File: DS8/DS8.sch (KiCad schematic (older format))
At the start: 92 parts, among them P1 CONN-02x05, Q1 3904, Q2 3904, U0 LM13700, U1 LM385, U2 LM385, U3 LM385, U4 LM385, U5 LM385, U6 KA78L05

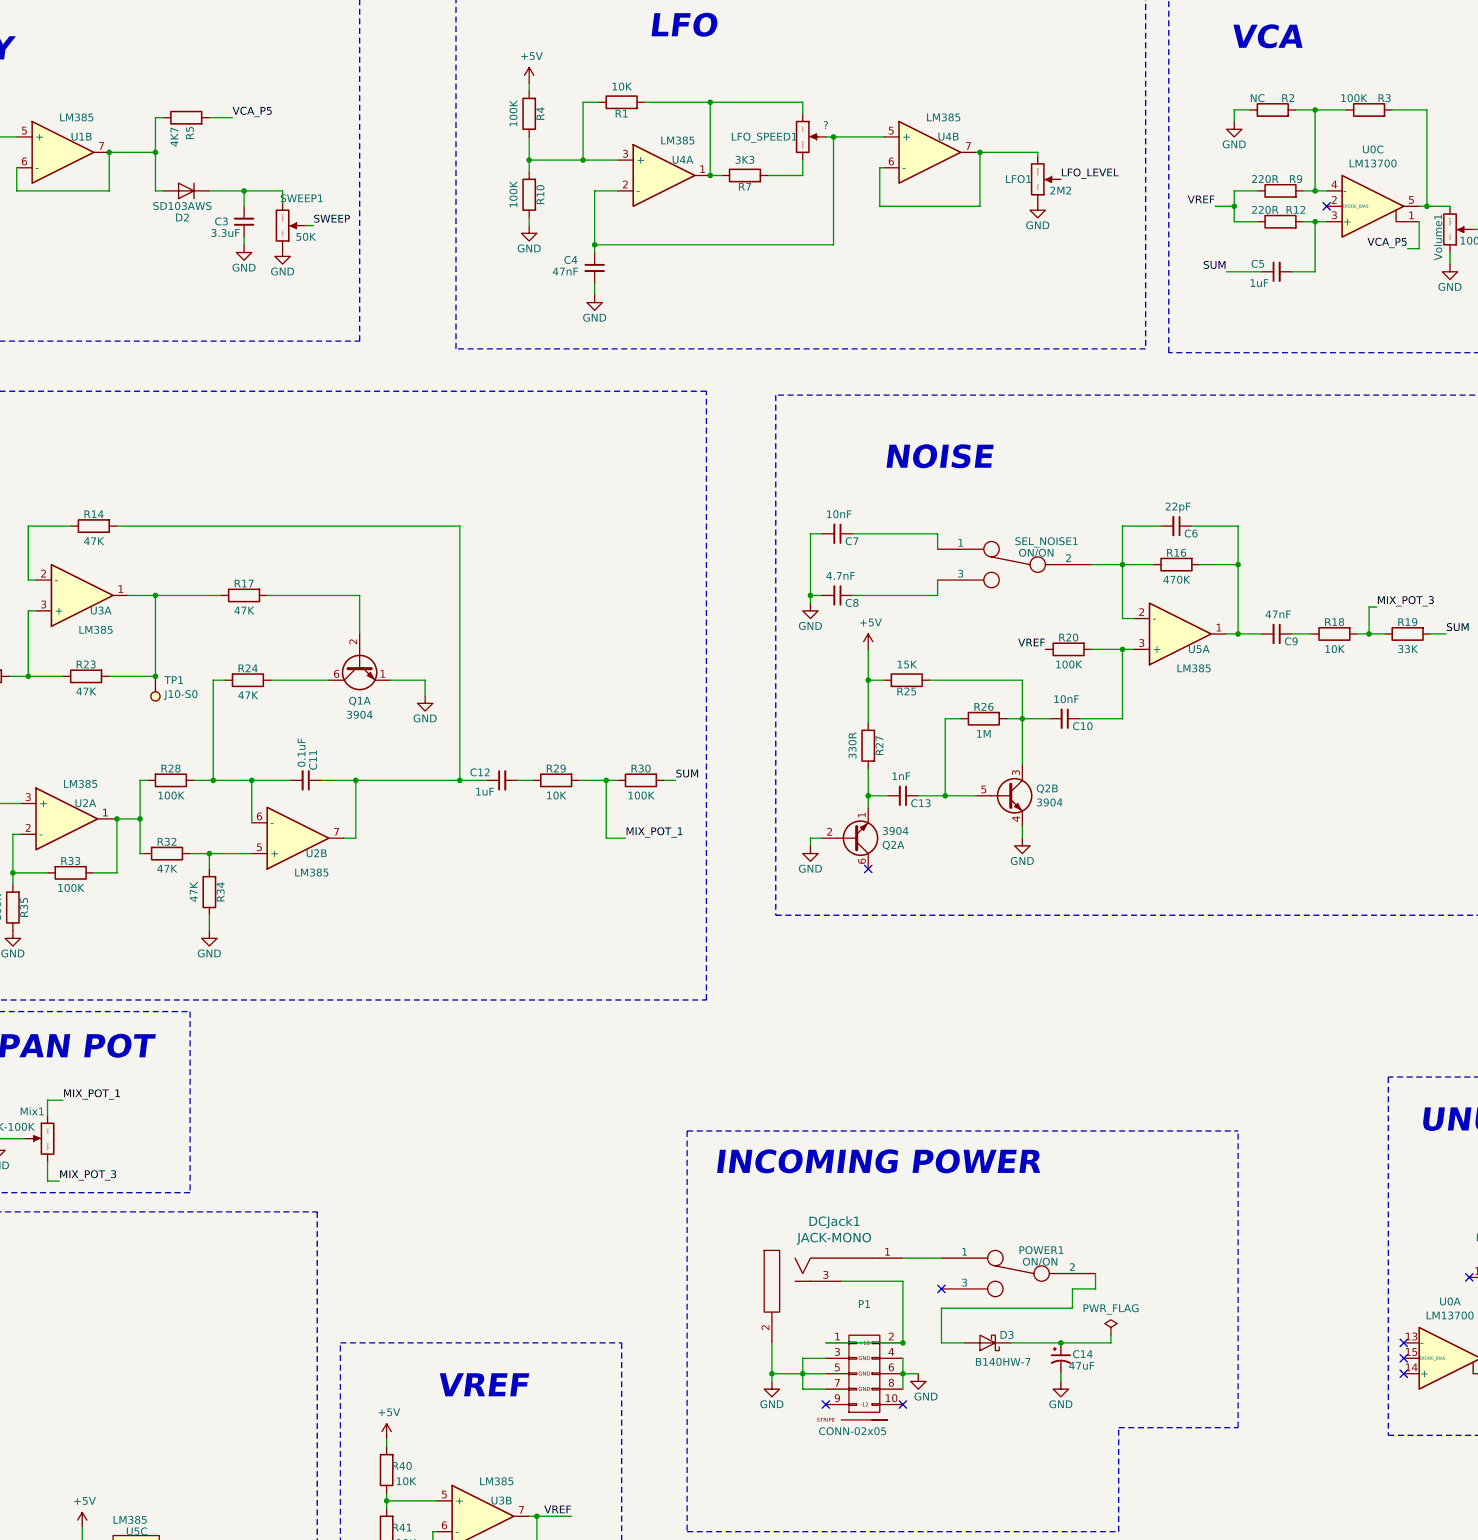
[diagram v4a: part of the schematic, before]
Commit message: Added test points for prototyping
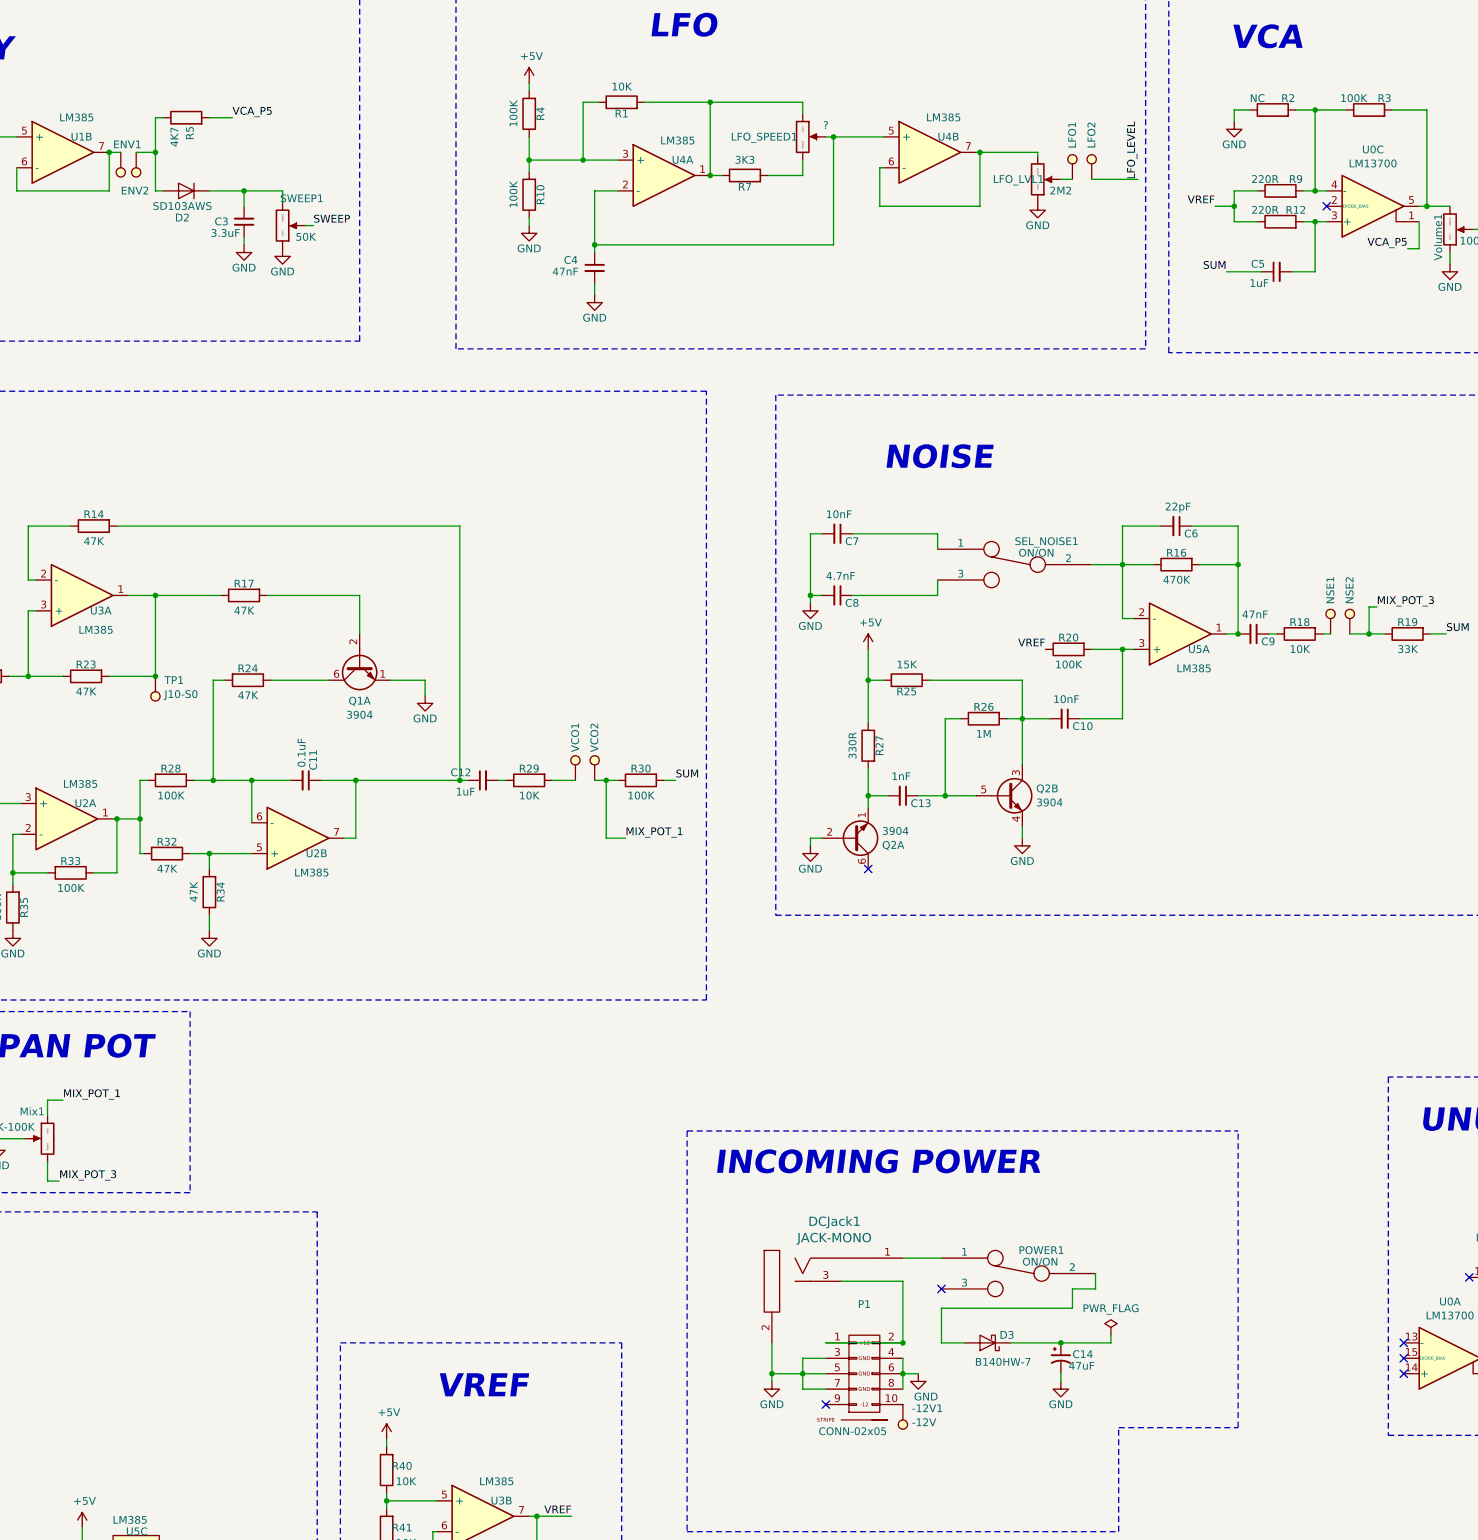
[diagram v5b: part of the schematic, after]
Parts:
- added -12V1: -12V, 4ms_TestPoint:TestPoint_WireHole, symbol 4ms-headers:Test_Point
- added ENV1, ENV2, LFO1, LFO2, NSE1, NSE2, VCO1, VCO2: TP, 4ms_TestPoint:TestPoint_Pad_10, symbol 4ms-headers:Test_Point
- renumbered LFO1 to LFO_LVL1
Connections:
- net LFO_LEVEL: now also LFO2.1; no longer LFO_LVL1.2 (Center)
- net MIX_POT_1: now also VCO2.1; no longer R29.2
- net MIX_POT_3: now also NSE2.1; no longer R18.2
- net at P1.10 (-12V): now also -12V1.1
- net at U1.6 (-), U1.7: now also ENV1.1; no longer D2.2 (A), R5.1
- new net: D2.2 (A), ENV2.1, R5.1
- new net: LFO1.1, LFO_LVL1.2 (Center)
- new net: R29.2, VCO1.1
- new net: NSE1.1, R18.2
- no-connect marks 20 -> 19
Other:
- moved on the sheet: C12, C9, R18, R29

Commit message: Finished first draft of layout
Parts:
- removed Piezo1: JACK-MONO, 4ms_Jack:EighthInch_PJ398SM, symbol 4ms-mech:JACK-MONO
- removed TP1: J10-S0, 4ms_TestPoint:TestPoint_WireHole, symbol 4ms-headers:Test_Point
- added PIEZO1, PIEZO2: TP, 4ms_TestPoint:TestPoint_WireHole, symbol 4ms-headers:Test_Point
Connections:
- net GND: now also PIEZO2.1
- net at Trigger_In1.3 (SW): now also PIEZO1.1
- no-connect marks 19 -> 18
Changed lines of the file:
@@
 	6200 4475 6800 4475
-$Comp
-L 4ms-headers:Test_Point TP1
-U 1 1 5F0C5CB9
-P 5475 5000
-F 0 "TP1" H 5417 5026 50  0000 R CNN
-F 1 "J10-S0" H 5417 5117 50  0000 R CNN
-F 2 "4ms_TestPoint:TestPoint_WireHole" H 5675 5000 50  0001 C CNN
-F 3 "" H 5675 5000 50  0001 C CNN
-	1    5475 5000
-	-1   0    0    1
-$EndComp
-Connection ~ 5475 5000
 $Comp
 L 4ms-passives:R R?
@@
 	14725 2100 14775 2100
 $Comp
-L 4ms-mech:JACK-MONO INL?
-U 1 1 5E040806
-P 950 2275
-AR Path="/5B8C674E/5E040806" Ref="INL?"  Part="1"
-AR Path="/5E040806" Ref="Piezo1"  Part="1"
-AR Path="/5DCE035A/5E040806" Ref="INL?"  Part="1"
-F 0 "Piezo1" H 1156 2662 60  0000 C CNN
-F 1 "JACK-MONO" H 1156 2556 60  0000 C CNN
-F 2 "4ms_Jack:EighthInch_PJ398SM" H 950 2275 60  0001 C CNN
-F 3 "" H 950 2275 60  0000 C CNN
-F 4 "Mouser" H -600 -400 50  0001 C CNN "Manufacturer"
-F 5 "Substitution OK" H -600 -400 50  0001 C CNN "Comments"
-F 6 "2" H -600 -400 50  0001 C CNN "Points"
-	1    950  2275
-	1    0    0    -1
-$EndComp
-$Comp
 L 4ms-power:GND #PWR?
 U 1 1 5E0413E2
-P 750 2675
+P 1600 2350
 AR Path="/5B8C674E/5E0413E2" Ref="#PWR?"  Part="1"
 AR Path="/5E0413E2" Ref="#PWR0106"  Part="1"
 AR Path="/5DCE035A/5E0413E2" Ref="#PWR?"  Part="1"
-F 0 "#PWR0106" H 750 2425 50  0001 C CNN
-F 1 "GND" H 900 2600 50  0000 C CNN
-F 2 "" H 750 2675 50  0000 C CNN
-F 3 "" H 750 2675 50  0000 C CNN
-	1    750  2675
-	1    0    0    -1
-$EndComp
-NoConn ~ 1200 2275
+F 0 "#PWR0106" H 1600 2100 50  0001 C CNN
+F 1 "GND" H 1750 2275 50  0000 C CNN
+F 2 "" H 1600 2350 50  0000 C CNN
+F 3 "" H 1600 2350 50  0000 C CNN
+	1    1600 2350
+	1    0    0    -1
+$EndComp
 Wire Wire Line
 	1600 1150 1225 1150
@@
 	-1   0    0    1
 $EndComp
+$Comp
+L 4ms-headers:Test_Point PIEZO1
+U 1 1 5DFA64AD
+P 1600 2125
+F 0 "PIEZO1" V 1600 2575 50  0000 R CNN
+F 1 "TP" H 1650 2075 50  0001 R CNN
+F 2 "4ms_TestPoint:TestPoint_WireHole" H 1800 2125 50  0001 C CNN
+F 3 "" H 1800 2125 50  0001 C CNN
+	1    1600 2125
+	0    -1   -1   0
+$EndComp
+$Comp
+L 4ms-headers:Test_Point PIEZO2
+U 1 1 5DFAC996
+P 1600 2300
+F 0 "PIEZO2" V 1600 2750 50  0000 R CNN
+F 1 "TP" H 1650 2250 50  0001 R CNN
+F 2 "4ms_TestPoint:TestPoint_WireHole" H 1800 2300 50  0001 C CNN
+F 3 "" H 1800 2300 50  0001 C CNN
+	1    1600 2300
+	0    -1   -1   0
+$EndComp
+Wire Wire Line
+	1600 2300 1600 2350
 $EndSCHEMATC

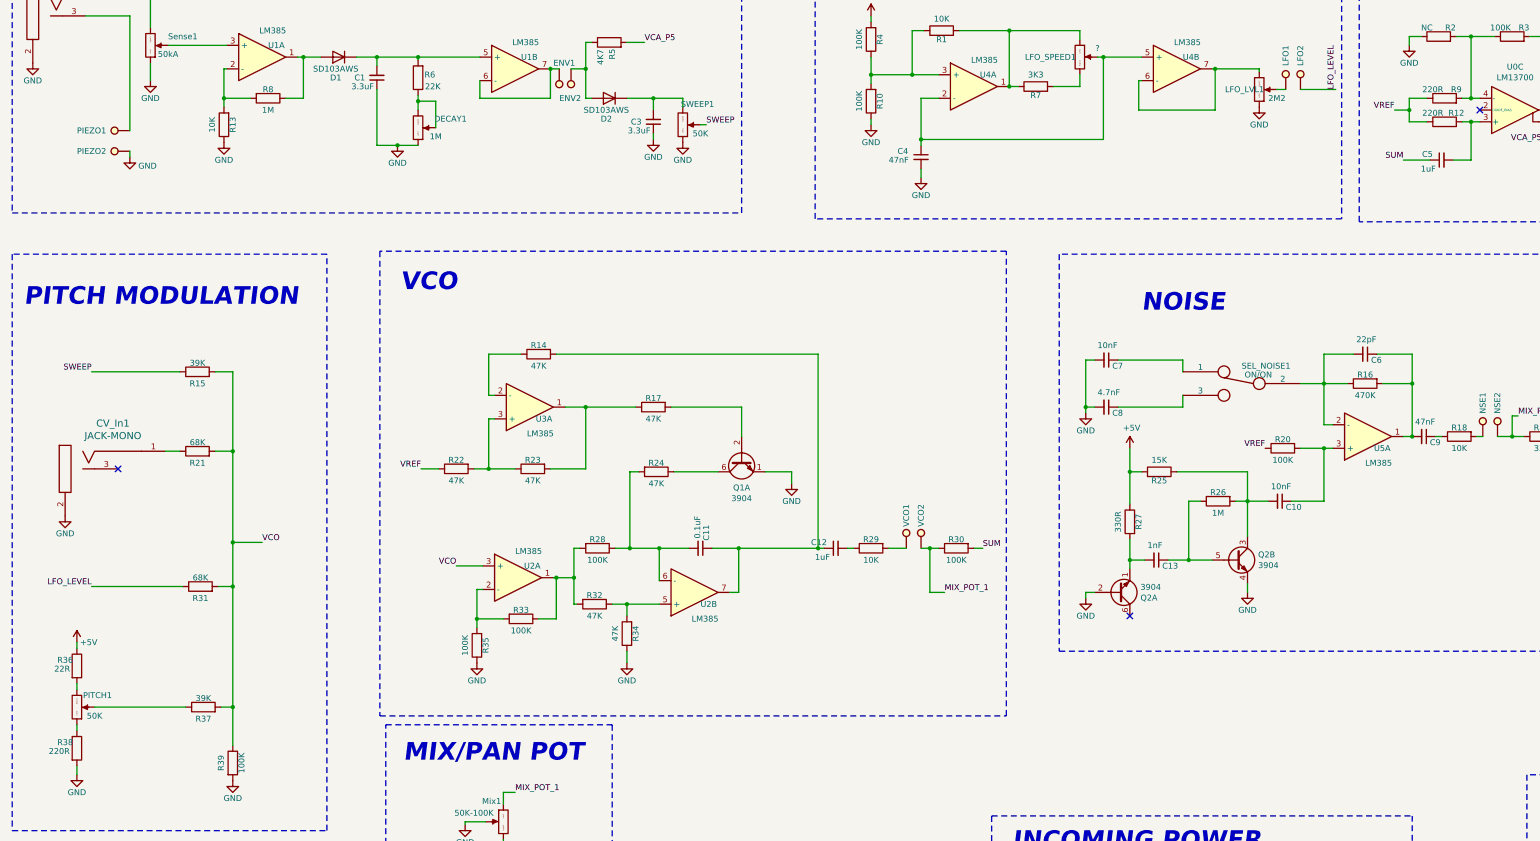
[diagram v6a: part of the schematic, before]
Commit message: redid GND - used tracks instead of GND plane - generated GERBERS
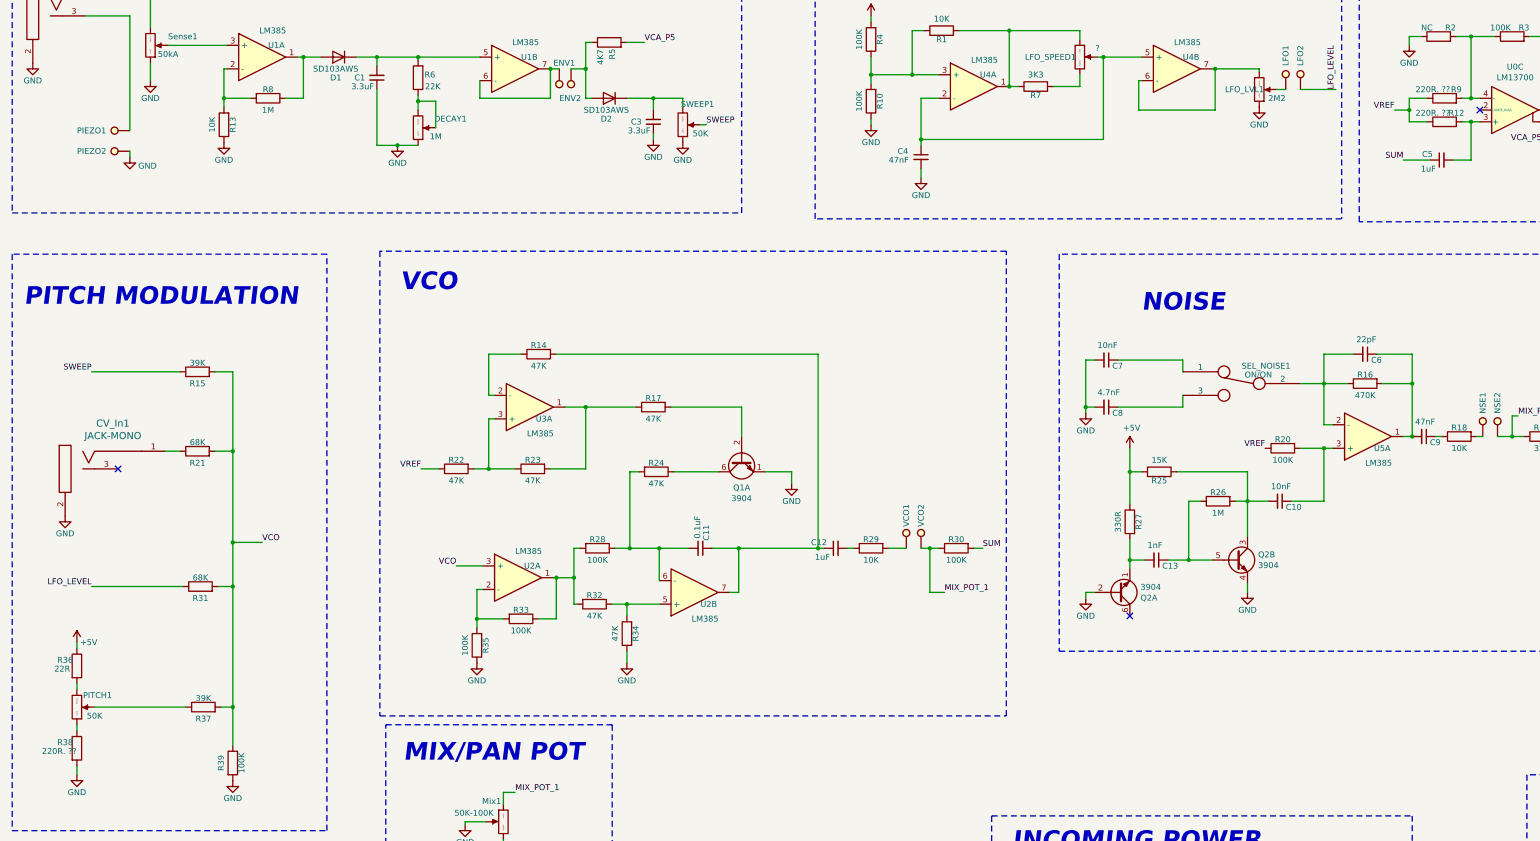
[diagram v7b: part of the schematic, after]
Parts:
- R12, R38, R9: value 220R -> 220R. ??
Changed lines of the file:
@@
 EESchema Schematic File Version 4
-LIBS:DS8-cache
 EELAYER 30 0
 EELAYER END
@@
 AR Path="/5DCE035A/5E6F260C" Ref="R?"  Part="1"
 F 0 "R38" H 1050 7425 50  0000 C CNN
-F 1 "220R" H 1000 7350 50  0000 C CNN
+F 1 "220R. ??" H 1000 7350 50  0000 C CNN
 F 2 "4ms_Resistor:R_0603" H 1150 7375 60  0001 C CNN
 F 3 "" H 1150 7375 60  0000 C CNN
@@
 AR Path="/5DCE035A/5EE8F66E" Ref="R?"  Part="1"
 F 0 "R9" V 12850 1750 50  0000 C CNN
-F 1 "220R" V 12850 1950 50  0000 C CNN
+F 1 "220R. ??" V 12850 1950 50  0000 C CNN
 F 2 "4ms_Resistor:R_0603" H 12775 1850 60  0001 C CNN
 F 3 "" H 12775 1850 60  0000 C CNN
@@
 AR Path="/5DCE035A/5EE901D2" Ref="R?"  Part="1"
 F 0 "R12" V 12850 1950 50  0000 C CNN
-F 1 "220R" V 12850 2150 50  0000 C CNN
+F 1 "220R. ??" V 12850 2150 50  0000 C CNN
 F 2 "4ms_Resistor:R_0603" H 12775 2050 60  0001 C CNN
 F 3 "" H 12775 2050 60  0000 C CNN

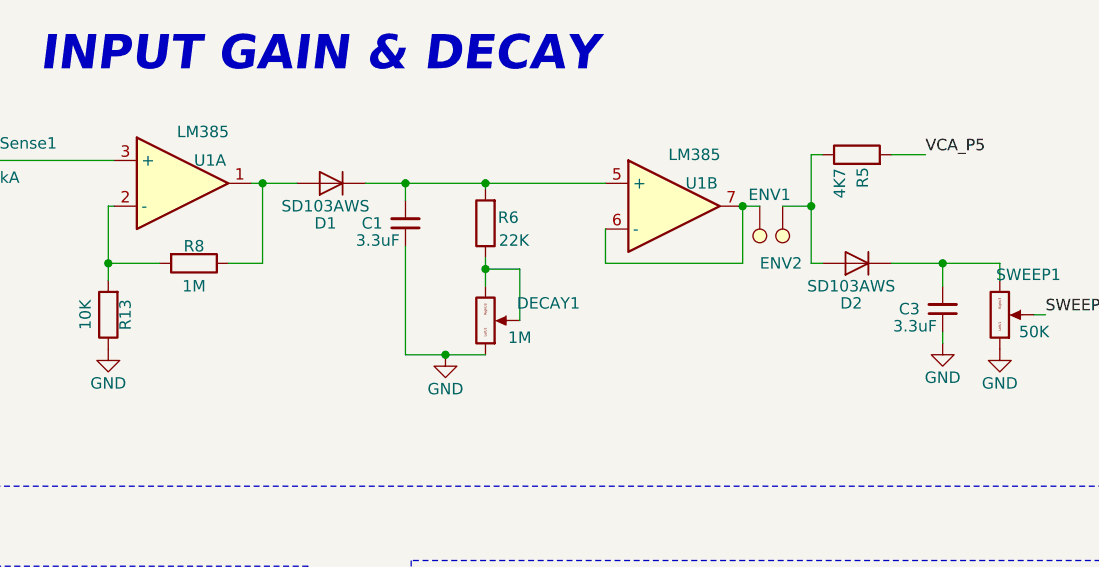
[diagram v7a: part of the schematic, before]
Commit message: updated decay caps on DS8 to 10uF
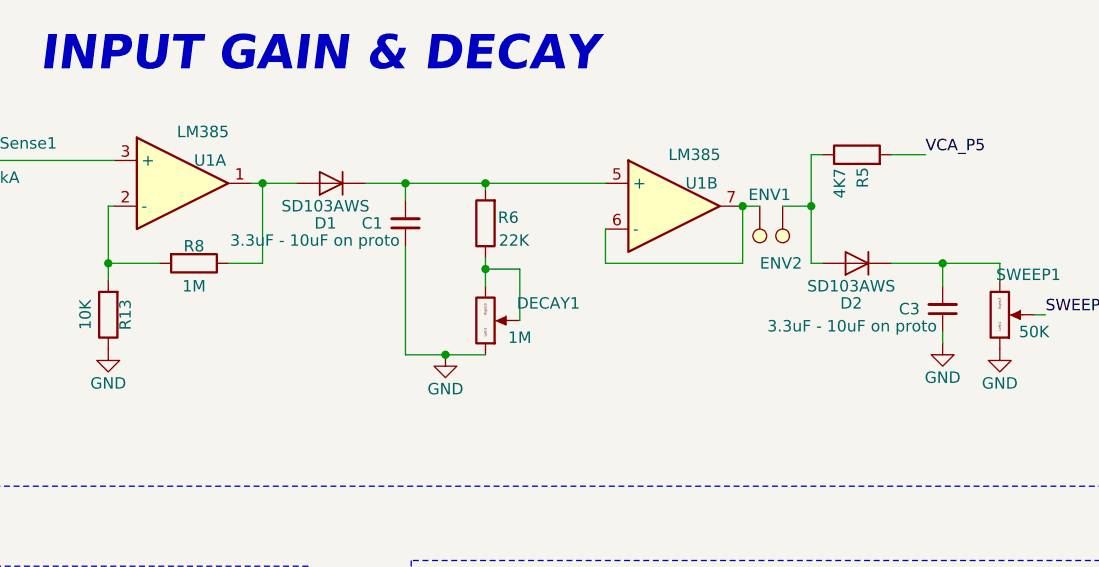
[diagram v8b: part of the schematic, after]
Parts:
- C1, C3: value 3.3uF -> 3.3uF - 10uF on proto
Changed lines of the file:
@@
 EESchema Schematic File Version 4
+LIBS:DS8-cache
 EELAYER 30 0
 EELAYER END
@@
 AR Path="/5DCE035A/5E16E6E0" Ref="C?"  Part="1"
 F 0 "C1" H 3800 1675 50  0000 L CNN
-F 1 "3.3uF" H 3725 1750 50  0000 L CNN
+F 1 "3.3uF - 10uF on proto" H 3725 1750 50  0000 L CNN
 F 2 "4ms_Capacitor:C_0805" H 3700 1675 50  0001 C CNN
 F 3 "" H 3700 1675 50  0000 C CNN
@@
 AR Path="/5DCE035A/5E286DAB" Ref="C?"  Part="1"
 F 0 "C3" H 6150 2050 50  0000 L CNN
-F 1 "3.3uF" H 6075 2125 50  0000 L CNN
+F 1 "3.3uF - 10uF on proto" H 6075 2125 50  0000 L CNN
 F 2 "4ms_Capacitor:C_0805" H 6050 2050 50  0001 C CNN
 F 3 "" H 6050 2050 50  0000 C CNN
